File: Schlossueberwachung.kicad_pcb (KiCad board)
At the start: 2 copper layers, 73.8 x 42 mm, 13 parts, among them J1 Conn_01x03_Male, J2 Conn_01x05_Male, J3 Conn_01x05_Male, Q101 BC847, U1 ATtiny13A-P, U2 TSOP348xx

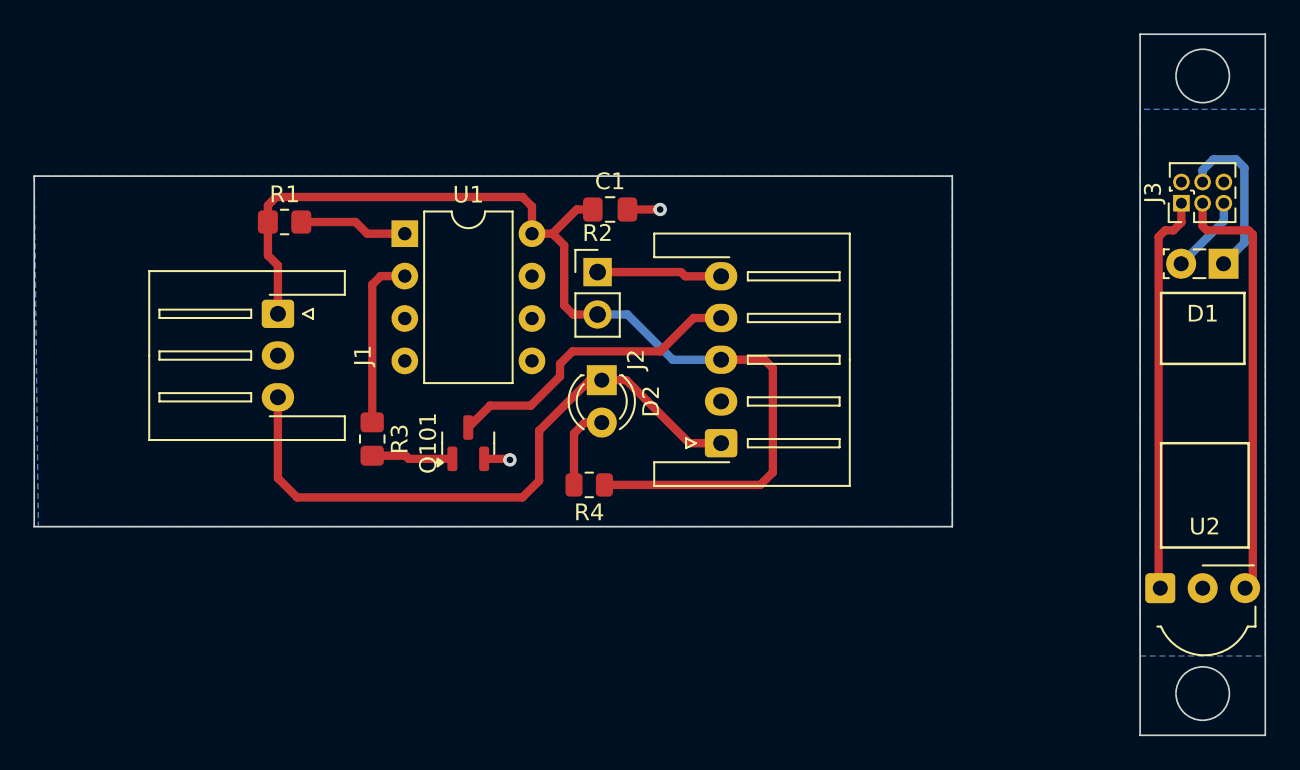
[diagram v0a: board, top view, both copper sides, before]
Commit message: modified connector placing
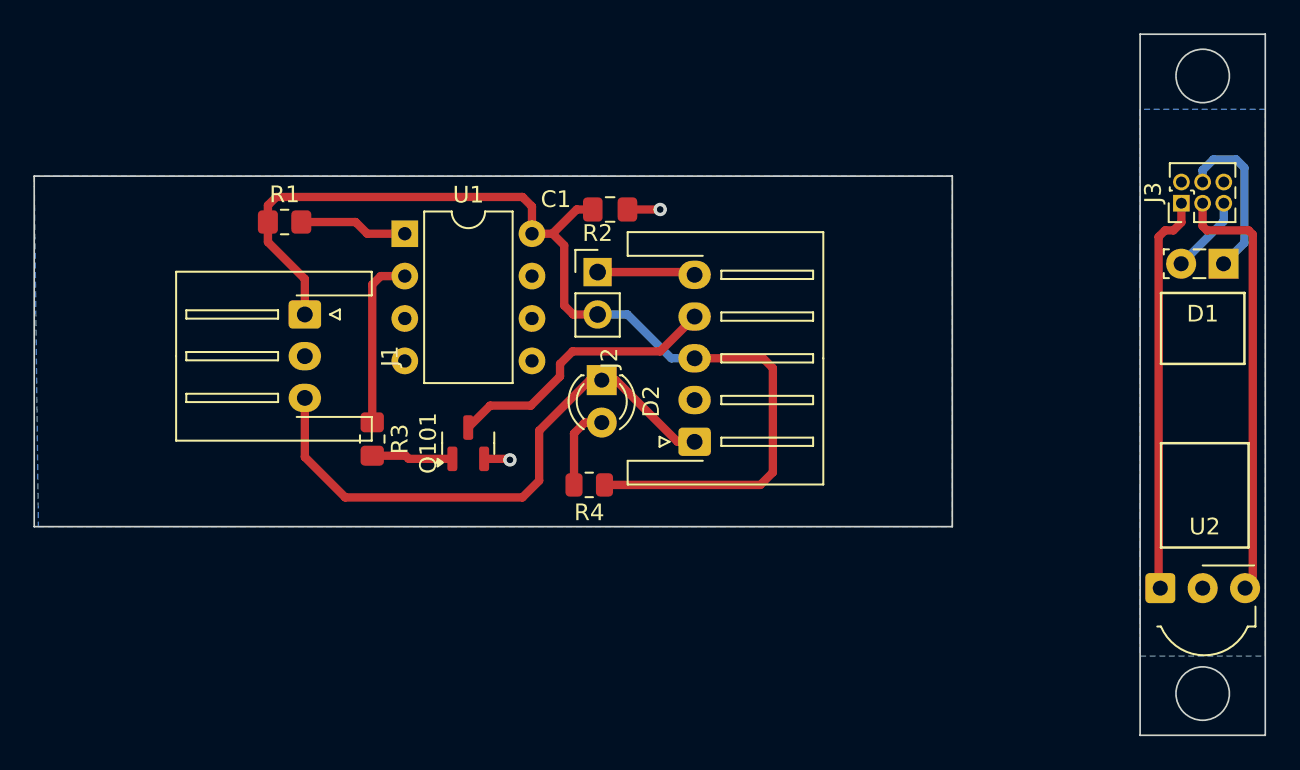
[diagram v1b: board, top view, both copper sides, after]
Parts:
- moved J1 1.61 mm to (96.2, 79.3)
- moved J2 1.59 mm to (119.6, 86.9)
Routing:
- net Lock: track 62.1 -> 58.1 mm
- net Emitter1-Cathode: track 18.3 -> 16.7 mm
- net Emitter1-Anode: track 7.50 -> 5.88 mm
- net VCC: track 90.1 -> 90.8 mm
